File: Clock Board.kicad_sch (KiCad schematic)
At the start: 20 parts, among them SW1 Micro Push SPST, SW2 SW_SPDT, U1 NE555P, U2 NE555P, U3 NE555P, U4 74HCT02, U5 74HCT02, U6 74LS08

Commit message: PCB Work
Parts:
- added C6, C7: 0.1uF, Capacitor_THT:C_Disc_D5.0mm_W2.5mm_P5.00mm, symbol Device:C_Small
- added D1, D2, D3: LED, LED_THT:LED_D5.0mm, symbol PCM_SL_Devices:LED
- added J2: Clk Output, Connector_PinSocket_2.54mm:PinSocket_2x03_P2.54mm_Vertical, symbol Connector_Generic:Conn_02x03_Odd_Even
- added J3: Clk Output, Connector_PinHeader_2.54mm:PinHeader_2x03_P2.54mm_Vertical, symbol Connector_Generic:Conn_02x03_Odd_Even
- added R7, R8, R9: 220, Resistor_THT:R_Axial_DIN0207_L6.3mm_D2.5mm_P10.16mm_Horizontal, symbol Device:R
- C1, C3, C4, C5: footprint (none) -> Capacitor_THT:C_Disc_D5.0mm_W2.5mm_P5.00mm
- C2: footprint (none) -> PCM_Capacitor_THT_AKL:CP_Radial_D5.0mm_P2.00mm
- R1, R2, R3, R4, R5, R6: footprint (none) -> Resistor_THT:R_Axial_DIN0207_L6.3mm_D2.5mm_P10.16mm_Horizontal
- RV1: footprint (none) -> Potentiometer_THT:Potentiometer_TT_P0915N
- SW1: value Micro Push SPST -> Single Step; footprint (none) -> digikey-footprints:Terminal_Block_D1.3mm_P5mm
- SW2: value SW_SPDT -> Clk Select; footprint (none) -> Button_Switch_THT:SW_Slide_SPDT_Straight_CK_OS102011MS2Q
- U1, U2, U3: footprint digikey-footprints:DIP-8_W7.62mm -> Package_DIP:DIP-8_W7.62mm_Socket
- U4, U6: footprint (none) -> Package_DIP:DIP-14_W7.62mm_Socket
- U4: renamed from U5; footprint (none) -> Package_DIP:DIP-14_W7.62mm_Socket
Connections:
- net GND: now also U4.7 (GND), U6.7 (GND), C6.2, C7.2, J2.5 (Pin_5), J2.6 (Pin_6), J3.5 (Pin_5), J3.6 (Pin_6), R7.2, R8.2, R9.1
- net VCC: now also U4.14 (VCC), U6.14 (VCC), C6.1, C7.1, J2.1 (Pin_1), J2.2 (Pin_2), J3.1 (Pin_1), J3.2 (Pin_2)
- net at U1.3 (OUT): now also U6.5, D2.1
- net at U2.3 (OUT): now also U6.1, D3.1
- net at U6.2: now also U3.3 (OUT), U4.11, U4.12
- net at U6.3: now also U4.8
- net at U6.4: now also U4.13
- net at U6.6: now also U4.9
- net at U4.4: now also D1.2, J2.3 (Pin_3), J2.4 (Pin_4), J3.3 (Pin_3), J3.4 (Pin_4)
- new net: D3.2, R9.2
- new net: D2.2, R8.1
- new net: D1.1, R7.1
- no-connect marks 3 -> 2
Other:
- moved on the sheet: C1, C2, C3, C4, C5, R1, R2, R3, R4, R5, R6, RV1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

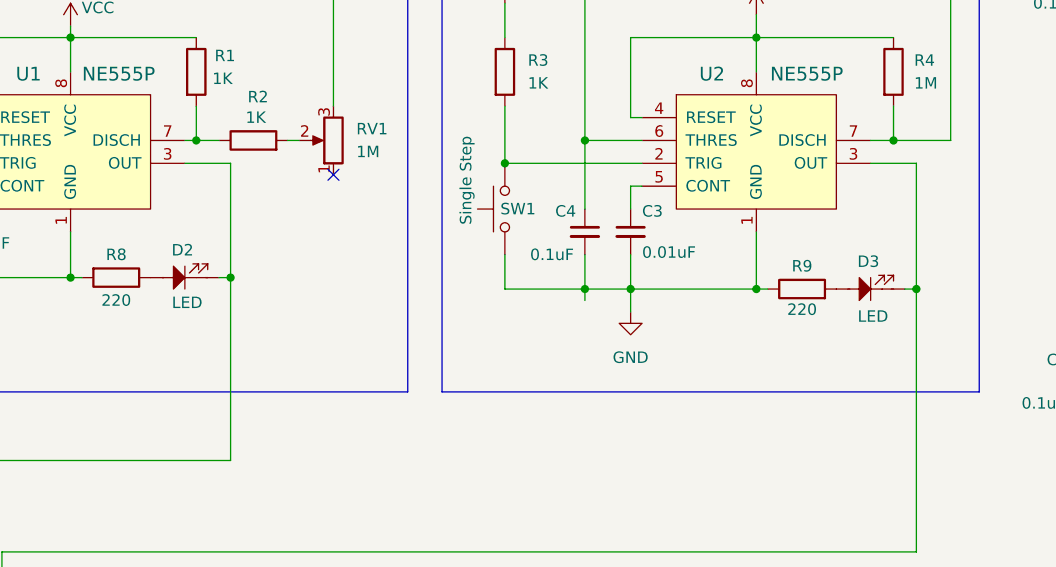
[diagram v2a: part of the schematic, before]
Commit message: Reverse diodes, increase text size on some labels
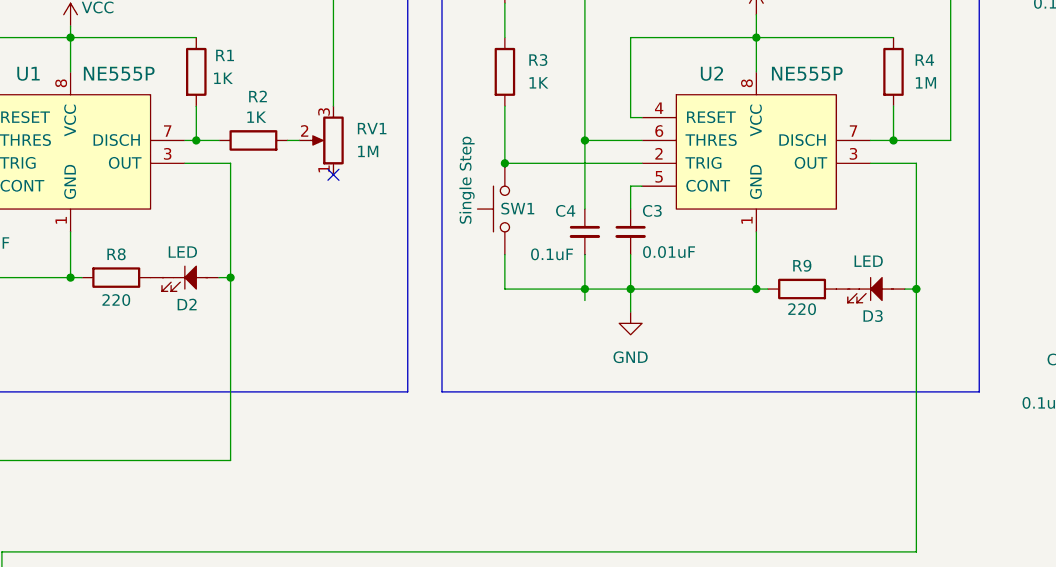
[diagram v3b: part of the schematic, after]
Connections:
- net at U1.3 (OUT), U6.5: now also D2.2; no longer D2.1
- net at U2.3 (OUT), U6.1: now also D3.2; no longer D3.1
- net at R9.2: now also D3.1; no longer D3.2
- net at R8.1: now also D2.1; no longer D2.2
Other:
- moved on the sheet: D2, D3
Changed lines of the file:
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@@
 	(symbol
 		(lib_id "PCM_SL_Devices:LED")
-		(at 215.9 80.01 0)
+		(at 215.9 80.01 180)
 		(unit 1)
 		(exclude_from_sim no)
@@
 		(dnp no)
 		(property "Reference" "D3"
+			(at 216.154 83.058 0)
+			(effects
+				(font
+					(size 1.27 1.27)
+				)
+			)
+		)
+		(property "Value" "LED"
 			(at 215.646 76.962 0)
 			(effects
@@
 			)
 		)
-		(property "Value" "LED"
-			(at 216.154 83.058 0)
-			(effects
-				(font
-					(size 1.27 1.27)
-				)
-			)
-		)
 		(property "Footprint" "LED_THT:LED_D5.0mm"
-			(at 214.884 82.804 0)
+			(at 216.916 77.216 0)
 			(effects
 				(font
@@
 		)
 		(property "Datasheet" ""
-			(at 214.63 80.01 0)
+			(at 217.17 80.01 0)
 			(effects
 				(font
@@
 	(symbol
 		(lib_id "PCM_SL_Devices:LED")
-		(at 139.7 78.74 0)
+		(at 139.7 78.74 180)
 		(unit 1)
 		(exclude_from_sim no)
@@
 		(dnp no)
 		(property "Reference" "D2"
-			(at 139.446 75.692 0)
+			(at 139.954 81.788 0)
 			(effects
 				(font
@@
 		)
 		(property "Value" "LED"
-			(at 139.954 81.534 0)
+			(at 139.446 75.946 0)
 			(effects
 				(font
@@
 		)
 		(property "Footprint" "LED_THT:LED_D5.0mm"
-			(at 138.684 81.534 0)
+			(at 140.716 75.946 0)
 			(effects
 				(font
@@
 		)
 		(property "Datasheet" ""
-			(at 138.43 78.74 0)
+			(at 140.97 78.74 0)
 			(effects
 				(font
